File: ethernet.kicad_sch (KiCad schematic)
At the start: 39 parts, among them J1001 7499010121A, U1001 LAN8742A-CZ-TR, U1002 USBLC6-4SC6

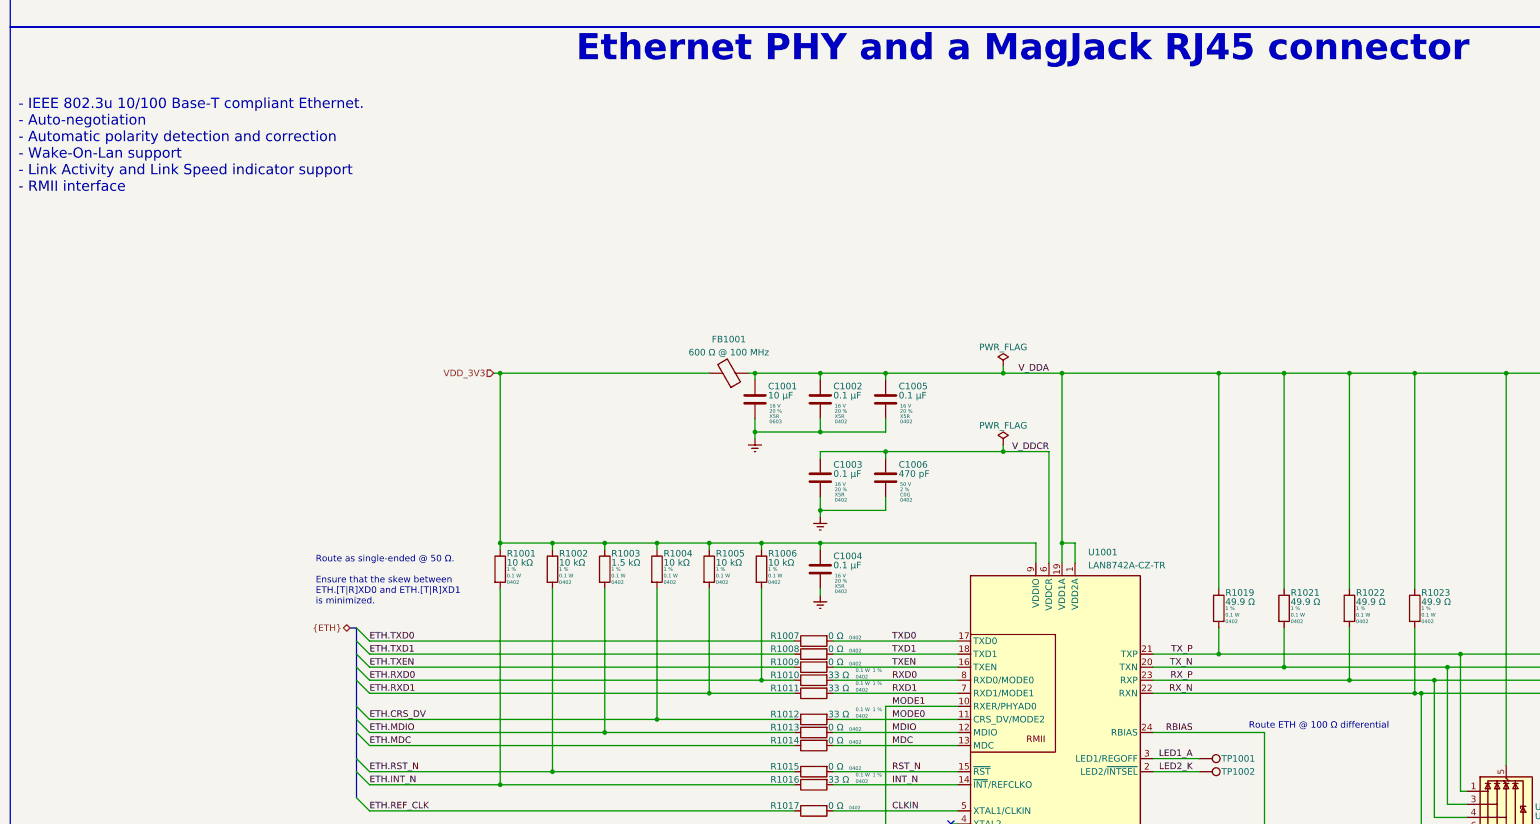
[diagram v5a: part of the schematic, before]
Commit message: Fill BOM information for the rest
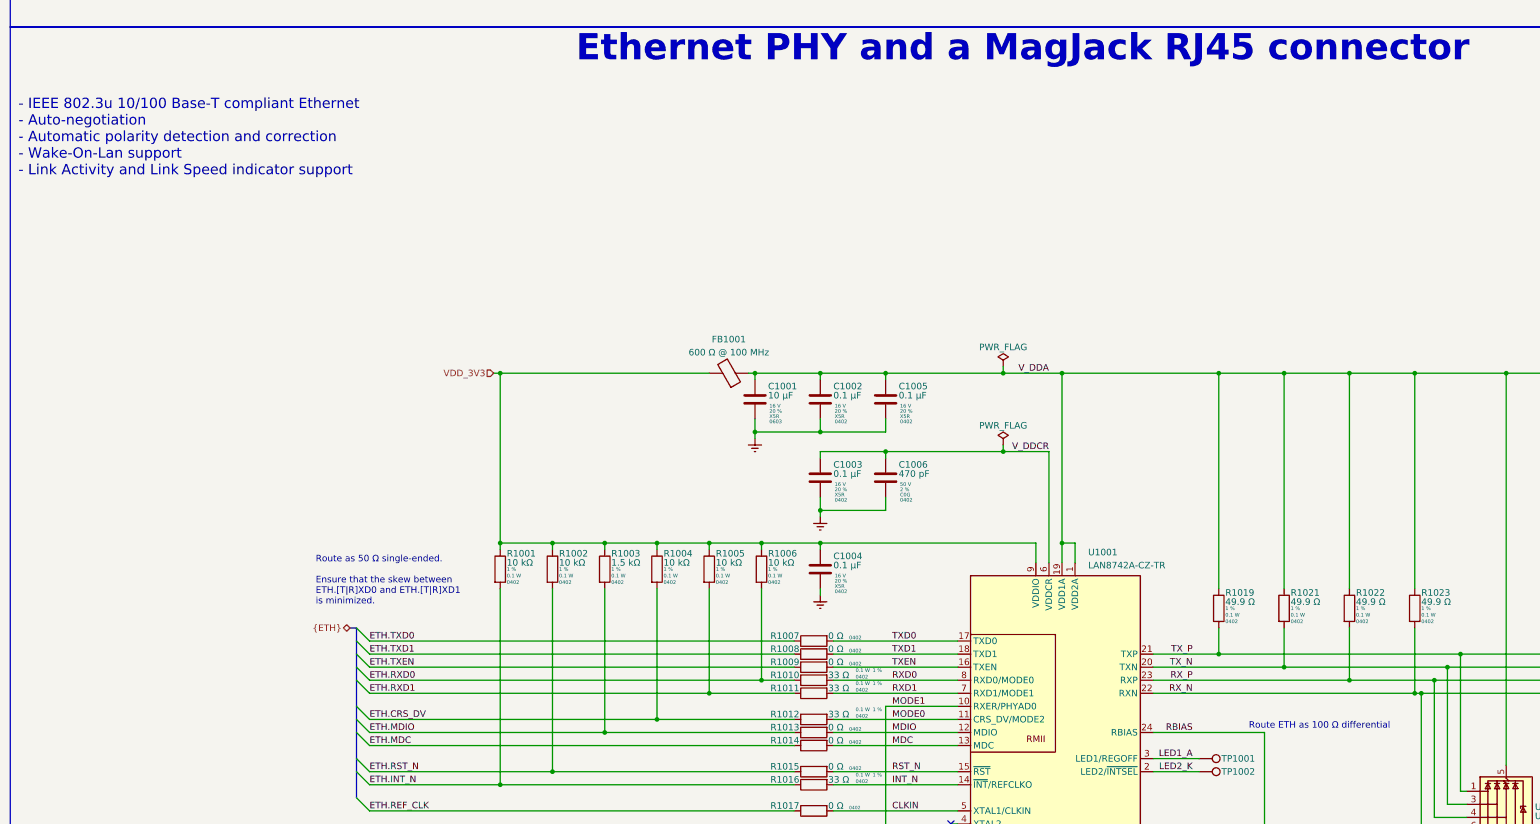
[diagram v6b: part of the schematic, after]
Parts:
- U1002: Digi-Key Part Number (none) -> 497-4492-1-ND; MPN (none) -> USBLC6-4SC6; Manufacturer (none) -> STMicroelectronics
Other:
- note added: "Route ETH as 100 Ω differential"
- note removed: "Route ETH @ 100 Ω differential"
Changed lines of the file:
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@@
 		)
 	)
-	(text "Route ETH @ 100 Ω differential"
+	(text "Route ETH as 100 Ω differential"
 		(exclude_from_sim no)
 		(at 253.492 186.69 0)
@@
 		)
 	)
-	(text_box "- IEEE 802.3u 10/100 Base-T compliant Ethernet.\n- Auto-negotiation\n- Automatic polarity detection and correction\n- Wake-On-Lan support\n- Link Activity and Link Speed indicator support\n- RMII interface"
+	(text_box "- IEEE 802.3u 10/100 Base-T compliant Ethernet\n- Auto-negotiation\n- Automatic polarity detection and correction\n- Wake-On-Lan support\n- Link Activity and Link Speed indicator support"
 		(exclude_from_sim no)
 		(at 13.335 63.5 0)
@@
 		)
 	)
-	(text_box "Route as single-ended @ 50 Ω.\n\nEnsure that the skew between ETH.[T|R]XD0 and ETH.[T|R]XD1 is minimized."
+	(text_box "Route as 50 Ω single-ended.\n\nEnsure that the skew between ETH.[T|R]XD0 and ETH.[T|R]XD1 is minimized."
 		(exclude_from_sim no)
 		(at 71.12 152.4 0)
@@
 			)
 		)
-		(property "Datasheet" "https://www.st.com/resource/en/datasheet/usblc6-4.pdf"
+		(property "Datasheet" "https://www.st.com/resource/en/datasheet/cd00047494.pdf"
 			(at 306.07 214.63 0)
 			(effects
@@
 			)
 		)
-		(property "Description" "Very low capacitance ESD protection diode, 4 data-line, SOT-23-6"
+		(property "Description" "17V Clamp 5A (8/20µs) Ipp Tvs Diode Surface Mount SOT-23-6"
+			(at 303.53 201.93 0)
+			(effects
+				(font
+					(size 1.27 1.27)
+				)
+				(hide yes)
+			)
+		)
+		(property "Digi-Key Part Number" "497-4492-1-ND"
+			(at 303.53 201.93 0)
+			(effects
+				(font
+					(size 1.27 1.27)
+				)
+				(hide yes)
+			)
+		)
+		(property "MPN" "USBLC6-4SC6"
+			(at 303.53 201.93 0)
+			(effects
+				(font
+					(size 1.27 1.27)
+				)
+				(hide yes)
+			)
+		)
+		(property "Manufacturer" "STMicroelectronics"
 			(at 303.53 201.93 0)
 			(effects

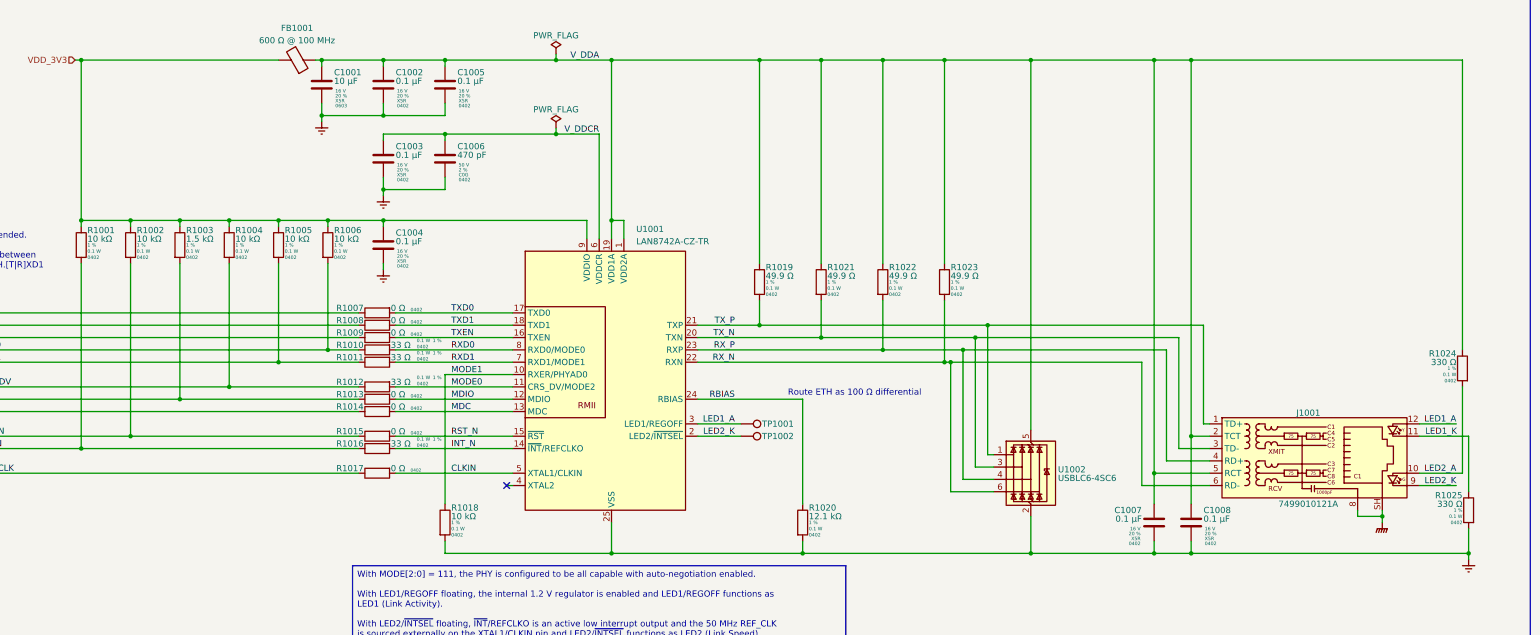
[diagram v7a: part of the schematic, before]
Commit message: 0402 -> 0201 where possible
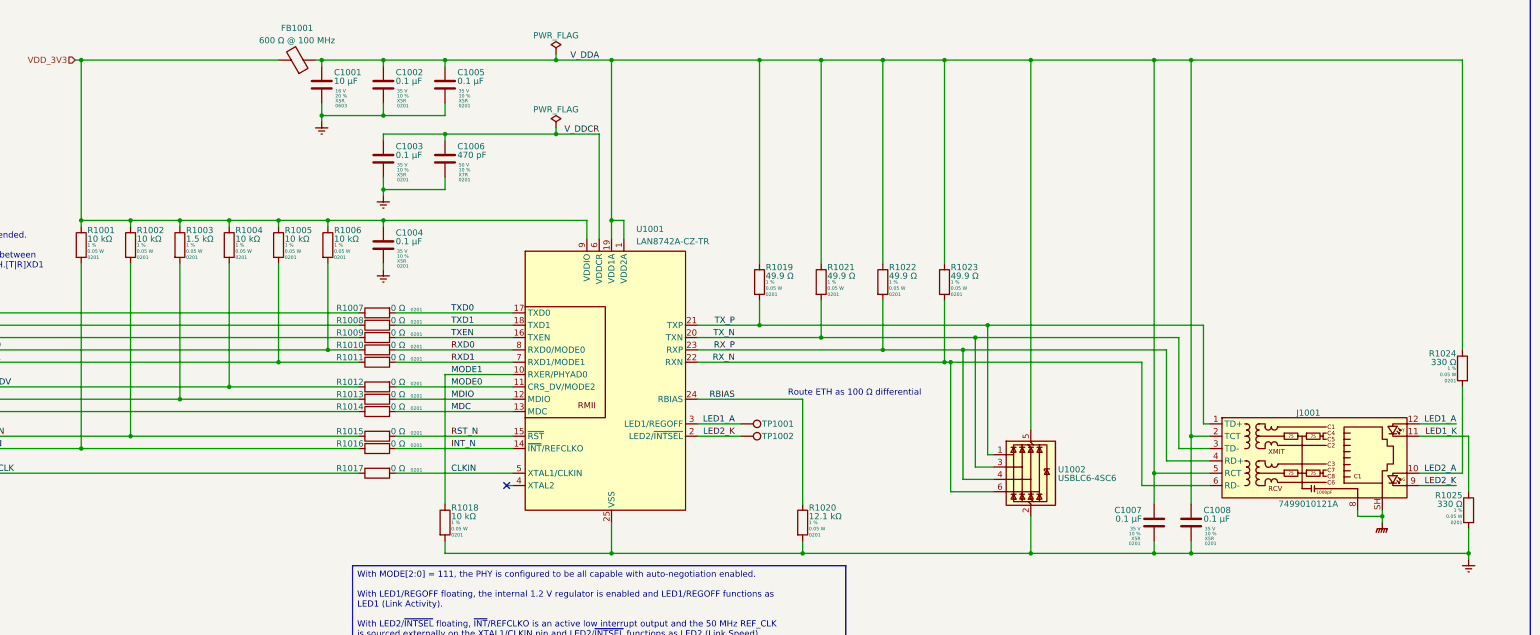
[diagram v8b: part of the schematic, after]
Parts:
- C1002, C1003, C1004, C1005, C1007, C1008: footprint perfect_footprints:C_0402_1005Metric -> Capacitor_SMD:C_0201_0603Metric; Digi-Key Part Number 490-10700-1-ND -> 490-10430-1-ND; MPN GRM155R71H104KE14D -> GRM033R6YA104KE14D; Size 0402 -> 0201; Tolerance 20 % -> 10 %; Voltage rating 16 V -> 35 V
- C1006: footprint perfect_footprints:C_0402_1005Metric -> Capacitor_SMD:C_0201_0603Metric; Digi-Key Part Number 490-1297-1-ND -> 490-12690-1-ND; MPN GRM1555C1H471JA01D -> GRM033R71H471KA12D; Size 0402 -> 0201; Temperature coefficient C0G -> X7R; Tolerance 2 % -> 10 %
- R1001, R1002, R1004, R1005, R1006, R1018: footprint perfect_footprints:R_0402_1005Metric -> Resistor_SMD:R_0201_0603Metric; Digi-Key Part Number P10.0KLCT-ND -> P122414CT-ND; MPN ERJ-2RKF1002X -> ERJ-1GNF1002C; Power rating 0.1 W -> 0.05 W; Size 0402 -> 0201
- R1003: footprint perfect_footprints:R_0402_1005Metric -> Resistor_SMD:R_0201_0603Metric; Digi-Key Part Number P1.50KLCT-ND -> P122743CT-ND; MPN ERJ-2RKF1501X -> ERJ-1GNF1501C; Power rating 0.1 W -> 0.05 W; Size 0402 -> 0201
- R1007, R1008, R1009, R1013, R1014, R1015, R1017: footprint perfect_footprints:R_0402_1005Metric -> Resistor_SMD:R_0201_0603Metric; Digi-Key Part Number P0.0JCT-ND -> P15979CT-ND; MPN ERJ-2GE0R00X -> ERJ-1GN0R00C; Size 0402 -> 0201
- R1010, R1011, R1012, R1016: value 33 Ω -> 0 Ω; footprint perfect_footprints:R_0402_1005Metric -> Resistor_SMD:R_0201_0603Metric; Digi-Key Part Number P33.0LCT-ND -> P15979CT-ND; MPN ERJ-2RKF33R0X -> ERJ-1GN0R00C; Power rating 0.1 W -> (none); Size 0402 -> 0201; Tolerance 1 % -> (none)
- R1019, R1021, R1022, R1023: footprint perfect_footprints:R_0402_1005Metric -> Resistor_SMD:R_0201_0603Metric; Digi-Key Part Number P49.9LCT-ND -> P123049CT-ND; MPN ERJ-2RKF49R9X -> ERJ-1GNF49R9C; Power rating 0.1 W -> 0.05 W; Size 0402 -> 0201
- R1020: footprint perfect_footprints:R_0402_1005Metric -> Resistor_SMD:R_0201_0603Metric; Digi-Key Part Number P12.1KLCT-ND -> P122698CT-ND; MPN ERJ-2RKF1212X -> ERJ-1GNF1212C; Power rating 0.1 W -> 0.05 W; Size 0402 -> 0201
- R1024, R1025: footprint perfect_footprints:R_0402_1005Metric -> Resistor_SMD:R_0201_0603Metric; Digi-Key Part Number 732-560112110231CT-ND -> P122936CT-ND; MPN 560112110231 -> ERJ-1GNF3300C; Manufacturer Würth Elektronik -> Panasonic Electronic Components; Power rating 0.1 W -> 0.05 W; Size 0402 -> 0201
